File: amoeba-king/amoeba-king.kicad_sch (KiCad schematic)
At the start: 8 parts

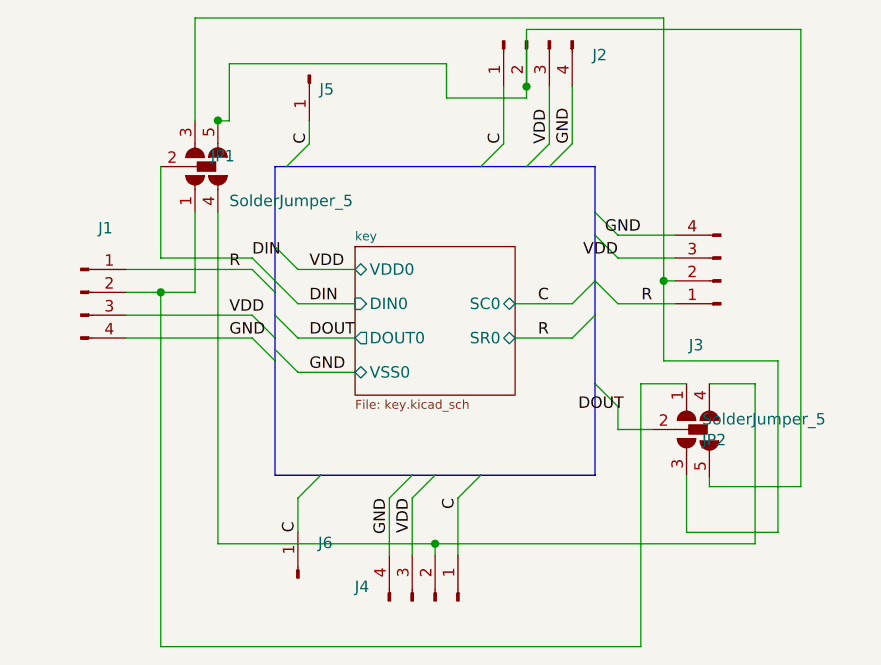
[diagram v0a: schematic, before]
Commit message: Added row via to be used as an anchor point for cabling.
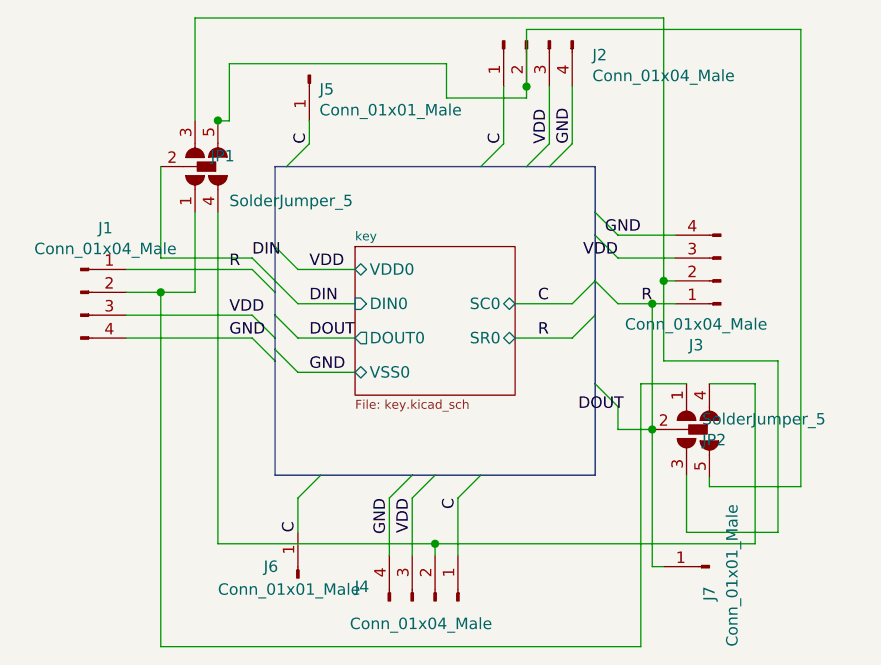
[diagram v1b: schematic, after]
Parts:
- added J7: Conn_01x01_Male, amoeba-modules:Header_1x01_P1.27mm, symbol Connector:Conn_01x01_Male
- J1, J4: value (none) -> Conn_01x04_Male; footprint (none) -> amoeba-modules:Header_1x04_P1.27mmL
- J2, J3: value (none) -> Conn_01x04_Male; footprint (none) -> amoeba-modules:Header_1x04_P1.27mm
- J5, J6: value (none) -> Conn_01x01_Male; footprint (none) -> amoeba-modules:Header_1x01_P1.27mm
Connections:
- net R: now also JP2.2 (C), J7.1 (Pin_1)
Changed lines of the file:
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@@
   (junction (at 135.89 107.95) (diameter 0) (color 0 0 0 0)
   )
+  (junction (at 160.02 81.28) (diameter 0) (color 0 0 0 0)
+  )
   (junction (at 111.7577 60.9205) (diameter 0) (color 0 0 0 0)
   )
+  (junction (at 160.02 95.25) (diameter 0) (color 0 0 0 0)
+  )
   (junction (at 161.29 78.74) (diameter 0) (color 0 0 0 0)
   )
@@
     (stroke (width 0) (type default) (color 0 0 0 0))
   )
-  (wire (pts (xy 156.21 81.28) (xy 162.56 81.28))
+  (wire (pts (xy 156.21 81.28) (xy 160.02 81.28))
     (stroke (width 0) (type default) (color 0 0 0 0))
   )
@@
     (stroke (width 0) (type default) (color 0 0 0 0))
   )
+  (wire (pts (xy 160.02 81.28) (xy 162.56 81.28))
+    (stroke (width 0) (type default) (color 0 0 0 0))
+  )
   (wire (pts (xy 176.53 101.6) (xy 166.37 101.6))
     (stroke (width 0) (type default) (color 0 0 0 0))
@@
     (stroke (width 0) (type default) (color 0 0 0 0))
   )
+  (wire (pts (xy 160.02 81.28) (xy 160.02 95.25))
+    (stroke (width 0) (type default) (color 0 0 0 0))
+  )
   (wire (pts (xy 160.02 95.25) (xy 156.21 95.25))
     (stroke (width 0) (type default) (color 0 0 0 0))
   )
+  (wire (pts (xy 160.02 95.25) (xy 160.02 110.49))
+    (stroke (width 0) (type default) (color 0 0 0 0))
+  )
   (wire (pts (xy 151.13 81.28) (xy 144.78 81.28))
     (stroke (width 0) (type default) (color 0 0 0 0))
@@
   )
   (bus (pts (xy 153.67 66.04) (xy 153.67 71.12))
+    (stroke (width 0) (type default) (color 0 0 0 0))
+  )
+  (wire (pts (xy 160.02 110.49) (xy 161.29 110.49))
     (stroke (width 0) (type default) (color 0 0 0 0))
   )
@@
       (effects (font (size 1.27 1.27)) (justify left))
     )
-    (property "Value" "" (id 1) (at 123.0376 59.7662 90)
-      (effects (font (size 1.27 1.27)) (justify left))
-    )
-    (property "Footprint" "" (id 2) (at 121.92 55.88 0)
+    (property "Value" "Conn_01x01_Male" (id 1) (at 123.0376 59.7662 90)
+      (effects (font (size 1.27 1.27)) (justify left))
+    )
+    (property "Footprint" "amoeba-modules:Header_1x01_P1.27mm" (id 2) (at 121.92 55.88 0)
       (effects (font (size 1.27 1.27)) hide)
     )
@@
   (symbol (lib_id "Connector:Conn_01x01_Male") (at 120.65 111.76 90) (unit 1)
     (in_bom yes) (on_board yes)
-    (property "Reference" "J6" (id 0) (at 122.8852 107.8484 90)
-      (effects (font (size 1.27 1.27)) (justify right))
-    )
-    (property "Value" "" (id 1) (at 122.8852 110.1598 90)
-      (effects (font (size 1.27 1.27)) (justify right))
-    )
-    (property "Footprint" "" (id 2) (at 120.65 111.76 0)
+    (property "Reference" "J6" (id 0) (at 116.84 110.49 90)
+      (effects (font (size 1.27 1.27)) (justify right))
+    )
+    (property "Value" "Conn_01x01_Male" (id 1) (at 111.76 113.03 90)
+      (effects (font (size 1.27 1.27)) (justify right))
+    )
+    (property "Footprint" "amoeba-modules:Header_1x01_P1.27mm" (id 2) (at 120.65 111.76 0)
       (effects (font (size 1.27 1.27)) hide)
     )
@@
     (in_bom yes) (on_board yes)
     (property "Reference" "J1" (id 0) (at 99.2632 72.8726 0))
-    (property "Value" "" (id 1) (at 99.2632 75.184 0))
-    (property "Footprint" "" (id 2) (at 96.52 80.01 0)
+    (property "Value" "Conn_01x04_Male" (id 1) (at 99.2632 75.184 0))
+    (property "Footprint" "amoeba-modules:Header_1x04_P1.27mmL" (id 2) (at 96.52 80.01 0)
       (effects (font (size 1.27 1.27)) hide)
     )
@@
       (effects (font (size 1.27 1.27)) (justify right))
     )
-    (property "Value" "" (id 1) (at 153.3652 55.9562 90)
-      (effects (font (size 1.27 1.27)) (justify right))
-    )
-    (property "Footprint" "" (id 2) (at 146.05 52.07 0)
+    (property "Value" "Conn_01x04_Male" (id 1) (at 153.3652 55.9562 90)
+      (effects (font (size 1.27 1.27)) (justify right))
+    )
+    (property "Footprint" "amoeba-modules:Header_1x04_P1.27mm" (id 2) (at 146.05 52.07 0)
       (effects (font (size 1.27 1.27)) hide)
     )
@@
     (in_bom yes) (on_board yes)
     (property "Reference" "J3" (id 0) (at 164.8968 85.8774 0))
-    (property "Value" "" (id 1) (at 164.8968 83.566 0))
-    (property "Footprint" "" (id 2) (at 167.64 78.74 0)
+    (property "Value" "Conn_01x04_Male" (id 1) (at 164.8968 83.566 0))
+    (property "Footprint" "amoeba-modules:Header_1x04_P1.27mm" (id 2) (at 167.64 78.74 0)
       (effects (font (size 1.27 1.27)) hide)
     )
@@
       (effects (font (size 1.27 1.27)) (justify right))
     )
-    (property "Value" "" (id 1) (at 128.5748 110.4138 90)
-      (effects (font (size 1.27 1.27)) (justify right))
-    )
-    (property "Footprint" "" (id 2) (at 135.89 114.3 0)
+    (property "Value" "Conn_01x04_Male" (id 1) (at 142.24 116.84 90)
+      (effects (font (size 1.27 1.27)) (justify right))
+    )
+    (property "Footprint" "amoeba-modules:Header_1x04_P1.27mmL" (id 2) (at 135.89 114.3 0)
       (effects (font (size 1.27 1.27)) hide)
     )
@@
     (pin "3")
     (pin "4")
+  )
+  (symbol (lib_id "Connector:Conn_01x01_Male") (at 166.37 110.49 180) (unit 1)
+    (in_bom yes) (on_board yes)
+    (property "Reference" "J7" (id 0) (at 166.37 114.3 90)
+      (effects (font (size 1.27 1.27)) (justify right))
+    )
+    (property "Value" "Conn_01x01_Male" (id 1) (at 168.91 119.38 90)
+      (effects (font (size 1.27 1.27)) (justify right))
+    )
+    (property "Footprint" "amoeba-modules:Header_1x01_P1.27mm" (id 2) (at 166.37 110.49 0)
+      (effects (font (size 1.27 1.27)) hide)
+    )
+    (property "Datasheet" "~" (id 3) (at 166.37 110.49 0)
+      (effects (font (size 1.27 1.27)) hide)
+    )
+    (pin "1")
   )
   (sheet (at 127 74.93) (size 17.78 16.51) (fields_autoplaced)
@@
       (reference "J6") (unit 1) (value "Conn_01x01_Male") (footprint "amoeba-modules:Header_1x01_P1.27mm")
     )
+    (path "/fac6d42b-0395-416b-9d7e-baf8f1e5e160"
+      (reference "J7") (unit 1) (value "Conn_01x01_Male") (footprint "amoeba-modules:Header_1x01_P1.27mm")
+    )
     (path "/00000000-0000-0000-0000-00005eceddd1"
